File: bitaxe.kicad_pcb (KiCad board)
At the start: 4 copper layers, 59.5 x 61.2 mm, 94 parts, among them IC1 BM1387, IC2 BM1387, IC3 MIC5317, IC4 MIC5317, J2 Conn_01x02, J3 Conn_01x05, J4 Conn_01x02, J5 Conn_01x03, Y1 25MHz

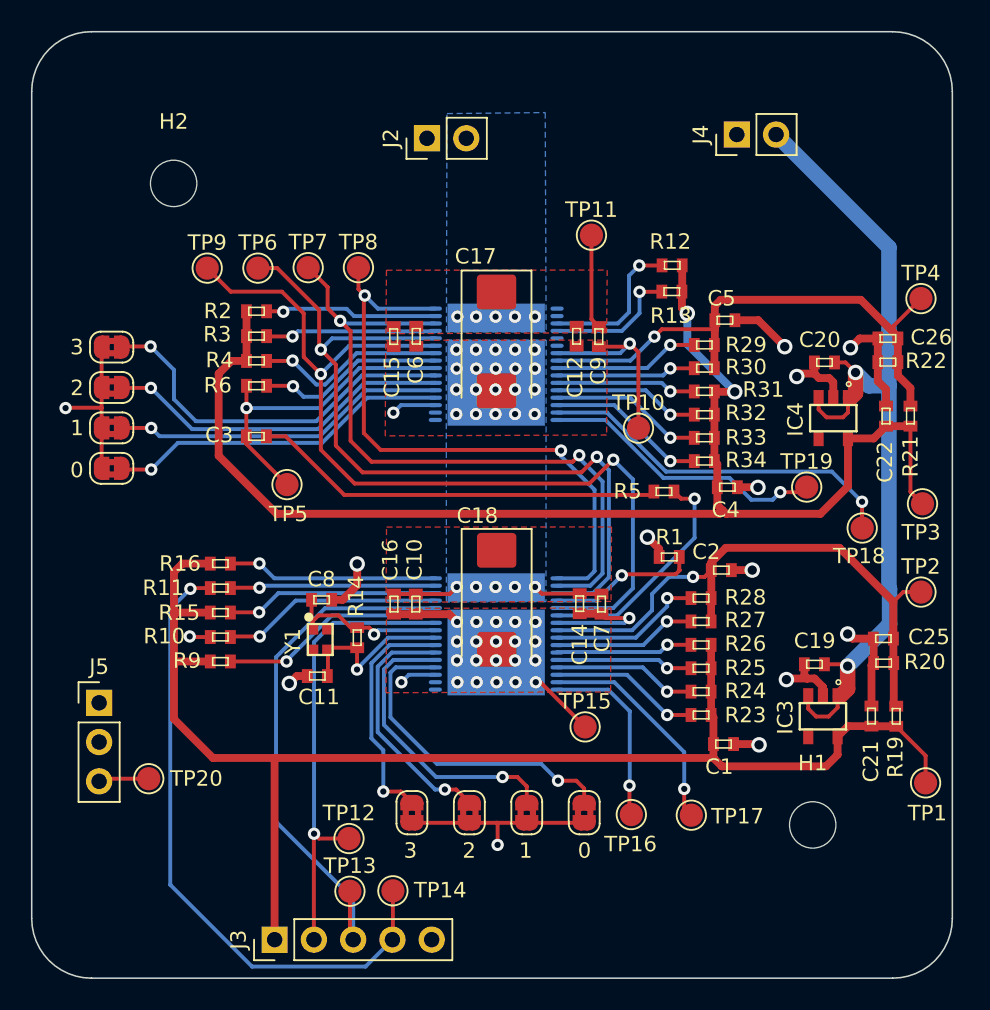
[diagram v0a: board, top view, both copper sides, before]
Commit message: updated silkscreen for #1. Added some 1.5mm alignment pin holes in the stencil and PCB
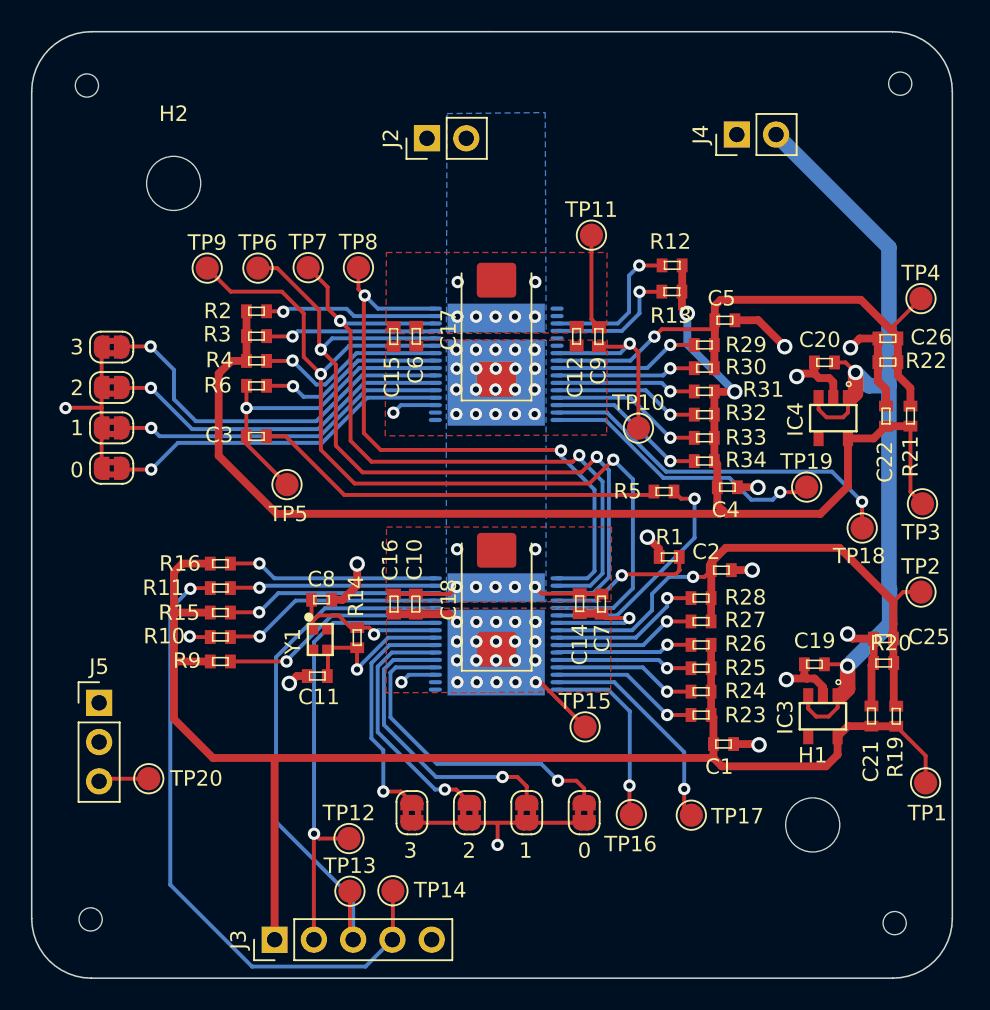
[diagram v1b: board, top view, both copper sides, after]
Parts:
- removed kibuzzard-6222FCD0: G***, kibuzzard-6222FCD0
- added H3: AlignmentHole, DayMiner:alignment_pin_1.5mm, F.Cu at (115.4, 49.5)
- added H4: AlignmentHole, DayMiner:alignment_pin_1.5mm, F.Cu at (115.1, 103.8)
- added H5: AlignmentHole, DayMiner:alignment_pin_1.5mm, F.Cu at (62.8, 49.6)
- added H6: AlignmentHole, DayMiner:alignment_pin_1.5mm, F.Cu at (63.1, 103.5)
- added kibuzzard-62A3C9C0: G***, kibuzzard-62A3C9C0, B.Cu at (92.7, 104.8)
- C17, C18: footprint Capacitor_Tantalum_SMD:CP_EIA-7343-31_Kemet-D_Pad2.25x2.55mm_HandSolder -> Capacitor_Tantalum_SMD:CP_EIA-7343-31_Kemet-D_Pad2.25x2.55mm_HandSolder_flip
- H1, H2: footprint MountingHole:MountingHole_3mm -> MountingHole:MountingHole_3.5mm
- R20: footprint DayMiner:C0402 -> DayMiner:R0402
- moved C17 0.76 mm to (89.3, 65.4), turned to 90 degrees
- turned C18 to 90 degrees
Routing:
- net /VIN: vias 5 -> 7
- net /A: vias 32 -> 34

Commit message: added VIN spade connectors for #6. moved the 5V pinheader around the corner. fixed the part numbers on R19-R22. Switched to in-stock LDOs for IC4 and IC5
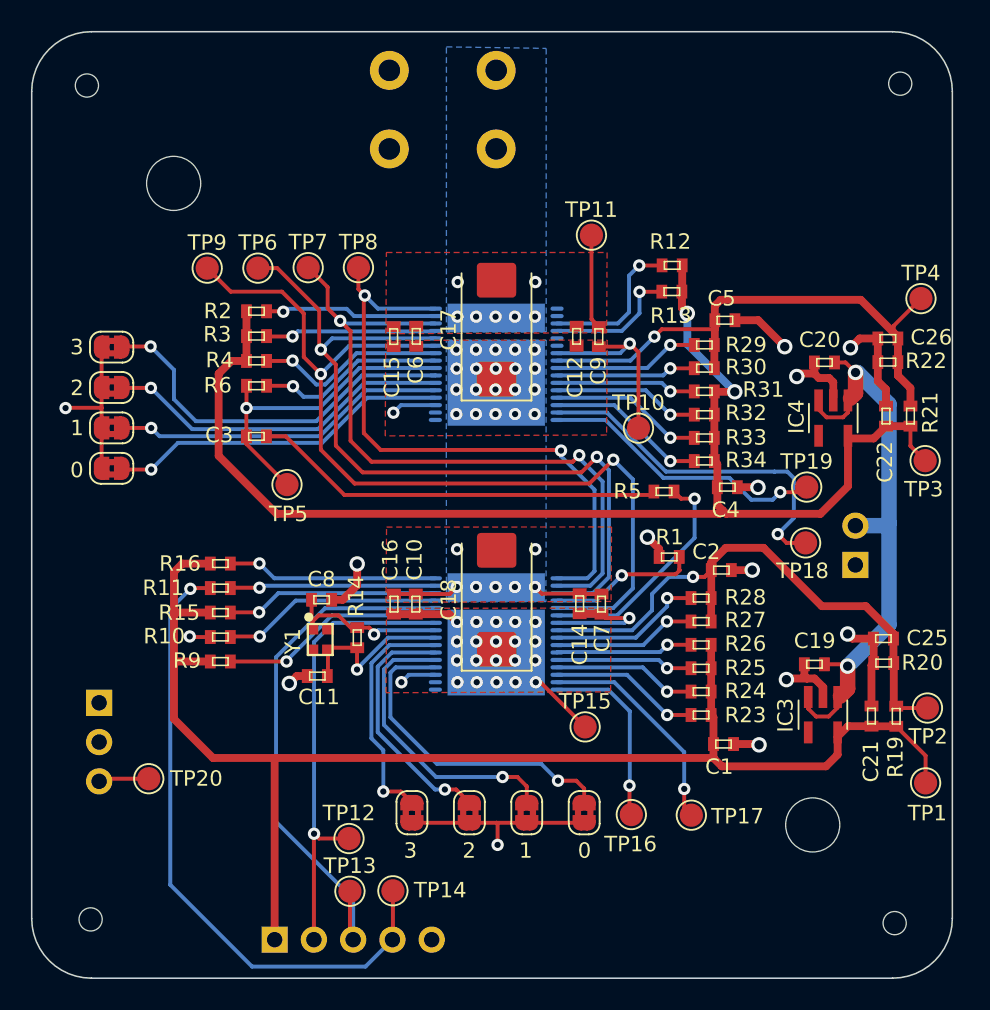
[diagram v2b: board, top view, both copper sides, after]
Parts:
- added J1: Conn_01x01, DayMiner:63862-1, B.Cu at (89.3, 51.2)
- C19, C20: value 1uF -> 311-3342-1-ND
- IC3, IC4: value MIC5317 -> TCR2EF18; footprint DayMiner:SOT23-5 -> DayMiner:TCR2EF18
- J2: value Conn_01x02 -> Conn_01x01; footprint Connector_PinHeader_2.54mm:PinHeader_1x02_P2.54mm_Vertical -> DayMiner:63862-1; moved to B.Cu
- J3, J4, J5: moved to B.Cu
- R19, R21: value RMCF0402FT12K4CT-ND -> 100
- R20, R22: value RMCF0402FT10K0CT-ND -> 100
- moved J4 28.9 mm to (112.5, 80.6), turned to 0 degrees
- moved TP2 7.51 mm to (117.2, 89.9)
- moved TP18 3.78 mm to (109.3, 79.2)
- moved J2 3.06 mm to (82.4, 51.2)
- moved TP3 2.80 mm to (117.0, 73.9)
- moved IC3 0.10 mm to (110.4, 90.3), turned to -90 degrees
- turned IC4 to -90 degrees
- turned J3 to -90 degrees
- turned J5 to 180 degrees
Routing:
- net /5V: track 106.8 -> 89.0 mm
- net /1V8_1: track 85.5 -> 82.8 mm
- net /0V8_2: track 38.5 -> 37.3 mm
- net Net-(IC1-Pad15): track 23.8 -> 23.2 mm

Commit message: added v2 BOM and gerbers
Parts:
- added TP21: TestPoint, TestPoint:TestPoint_Pad_D1.5mm, F.Cu at (100.2, 56.3)
- added TP22: TestPoint, TestPoint:TestPoint_Pad_D1.5mm, F.Cu at (104.5, 56.4)
- added TP23: TestPoint, TestPoint:TestPoint_Pad_D1.5mm, F.Cu at (105.7, 61.2)
- added TP24: TestPoint, TestPoint:TestPoint_Pad_D1.5mm, F.Cu at (110.2, 61.2)
- IC3, IC4: value TCR2EF18 -> SOT-25___SMV_TOS
- J5: footprint Connector_PinHeader_2.54mm:PinHeader_1x03_P2.54mm_Vertical -> Connector_Molex:Molex_KK-254_AE-6410-03A_1x03_P2.54mm_Vertical
- moved TP20 3.83 mm to (67.2, 98.3)
- moved J4 3.37 mm to (115.9, 80.7)
- moved TP3 0.80 mm to (116.6, 74.5)
- moved J5 0.27 mm to (63.4, 89.6), turned to -90 degrees
- moved H1 0.17 mm to (109.7, 97.3)
- moved H2 0.16 mm to (68.3, 55.9)
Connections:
- IC1 pad 1: unconnected-(IC1-Pad1) -> Net-(IC1-Pad1)
- IC1 pad 2: unconnected-(IC1-Pad2) -> Net-(IC1-Pad2)
- IC1 pad 5: unconnected-(IC1-Pad5) -> Net-(IC1-Pad5)
- IC1 pad 6: unconnected-(IC1-Pad6) -> Net-(IC1-Pad6)
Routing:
- net Net-(IC1-Pad6): track 0.00 -> 19.1 mm, vias 0 -> 1
- net Net-(IC1-Pad2): track 0.00 -> 15.5 mm, vias 0 -> 1
- net Net-(IC1-Pad5): track 0.00 -> 14.4 mm, vias 0 -> 1
- net Net-(IC1-Pad1): track 0.00 -> 12.7 mm, vias 0 -> 1
- net /PWM: track 3.28 -> 5.38 mm
- net /A: track 50.9 -> 52.1 mm
- net Net-(IC1-Pad23): track 24.6 -> 23.5 mm
- net /RO: track 35.2 -> 36.1 mm
- net /0V8_1: track 35.8 -> 36.7 mm
- net Net-(IC1-Pad3): track 9.74 -> 8.87 mm
- net Net-(IC1-Pad4): track 8.64 -> 7.86 mm
- net /5V: track 89.0 -> 88.3 mm
